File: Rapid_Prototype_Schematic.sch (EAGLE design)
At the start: 122 parts, among them IC1 OP-AMP, IC12 LM2904ITPX/NOPB, IC2 OP-AMP, IC3 OP-AMP, IC4 LM2904ITPX/NOPB, IC5 LM2904ITPX/NOPB, IC6 OP-AMP, IC7 OP-AMP

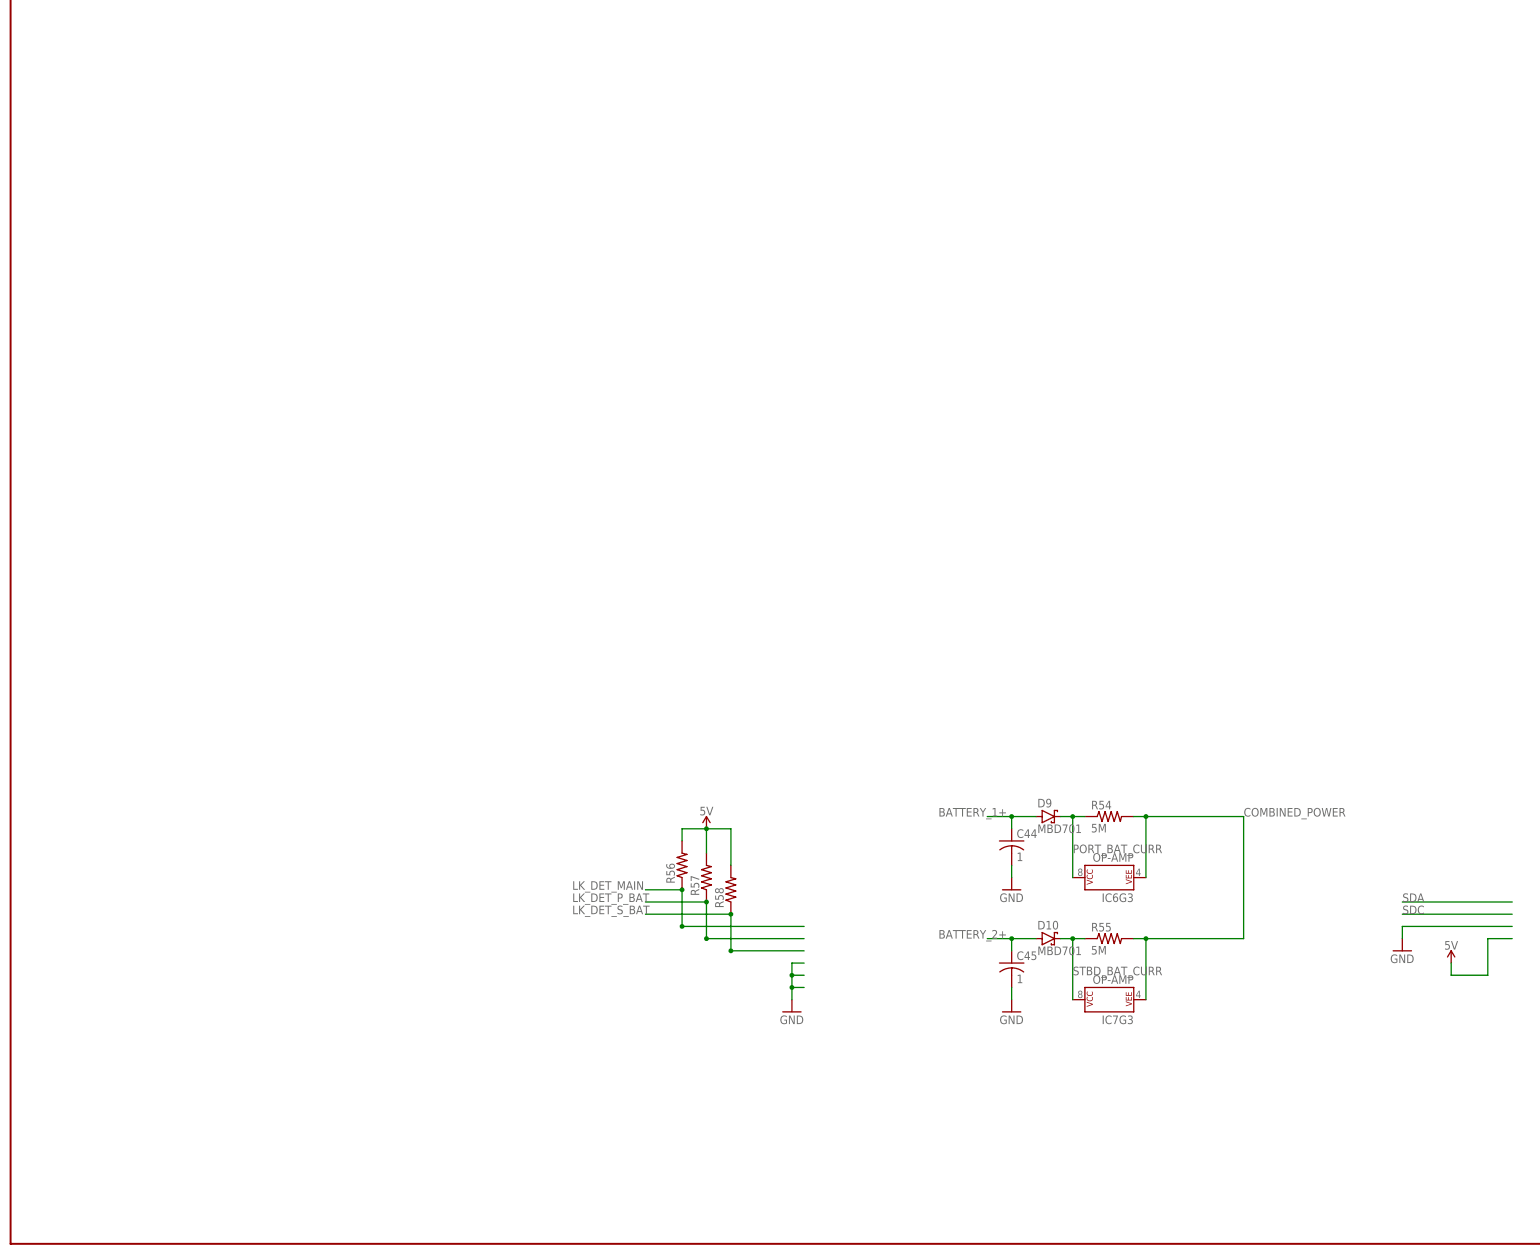
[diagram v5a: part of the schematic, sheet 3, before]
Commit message: Continued to work on the ESC modules and connected them up to each other
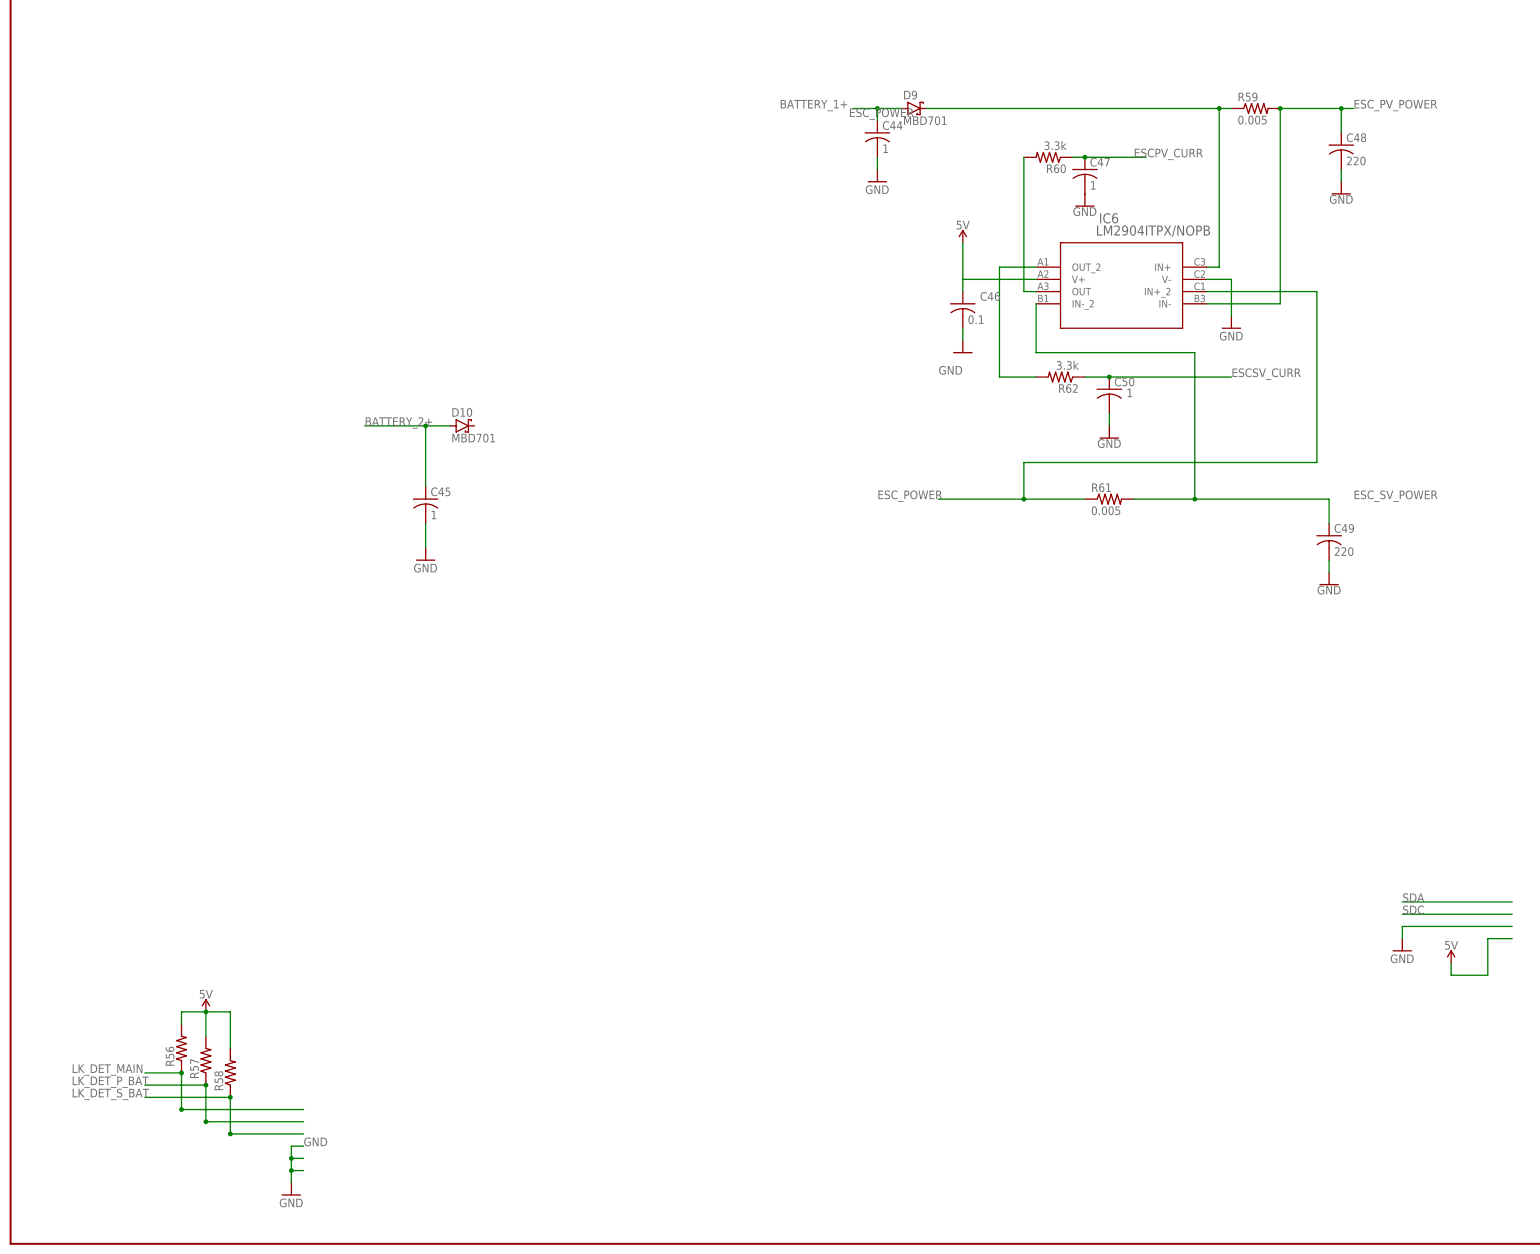
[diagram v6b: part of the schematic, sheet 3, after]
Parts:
- removed IC7: OP-AMP, SparkFun-IC-Amplifiers:OPAMP-DUALU
- removed R54, R55: 5M, adafruit:R-US_R0603
- added C46: 0.1, adafruit:C-USC0603
- added C47, C50: 1, adafruit:C-USC0805
- added C48, C49: 220, adafruit:C-US050-050X075
- added R59, R61: 0.005, adafruit:R-US_R1206
- added R60, R62: 3.3k, adafruit:R-US_R0603
- IC6: value OP-AMP -> LM2904ITPX/NOPB; device SparkFun-IC-Amplifiers:OPAMP-DUALU -> Opamp1:LM2904ITPX/NOPB
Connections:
- removed net PORT_BAT_CURR: D9.C, IC6G3.P$V+, R54.1
- removed net STBD_BAT_CURR: D10.C, IC7G3.P$V+, R55.1
- new net N$34: IC6.OUT, R60.2
- new net N$35: IC6.OUT_2, R62.2
- net 5V: now also C46.1, IC6.V+
- net COMBINED_POWER: no longer IC6G3.P$V-, IC7G3.P$V-, R54.2, R55.2
- net ESCPV_CURR: now also C47.1, R60.1
- net ESCSV_CURR: now also C50.1, R62.1
- net ESC_POWER: now also D9.C, IC6.IN+, IC6.IN+_2, R59.1, R61.1
- net ESC_PV_POWER: now also C48.1, IC6.IN-, R59.2
- net ESC_SV_POWER: now also C49.1, IC6.IN-_2, R61.2
- net GND: now also C46.2, C47.2, C48.2, C49.2, C50.2, IC6.V-
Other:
- moved on the sheet: C44, C45, D10, D9, R56, R57, R58

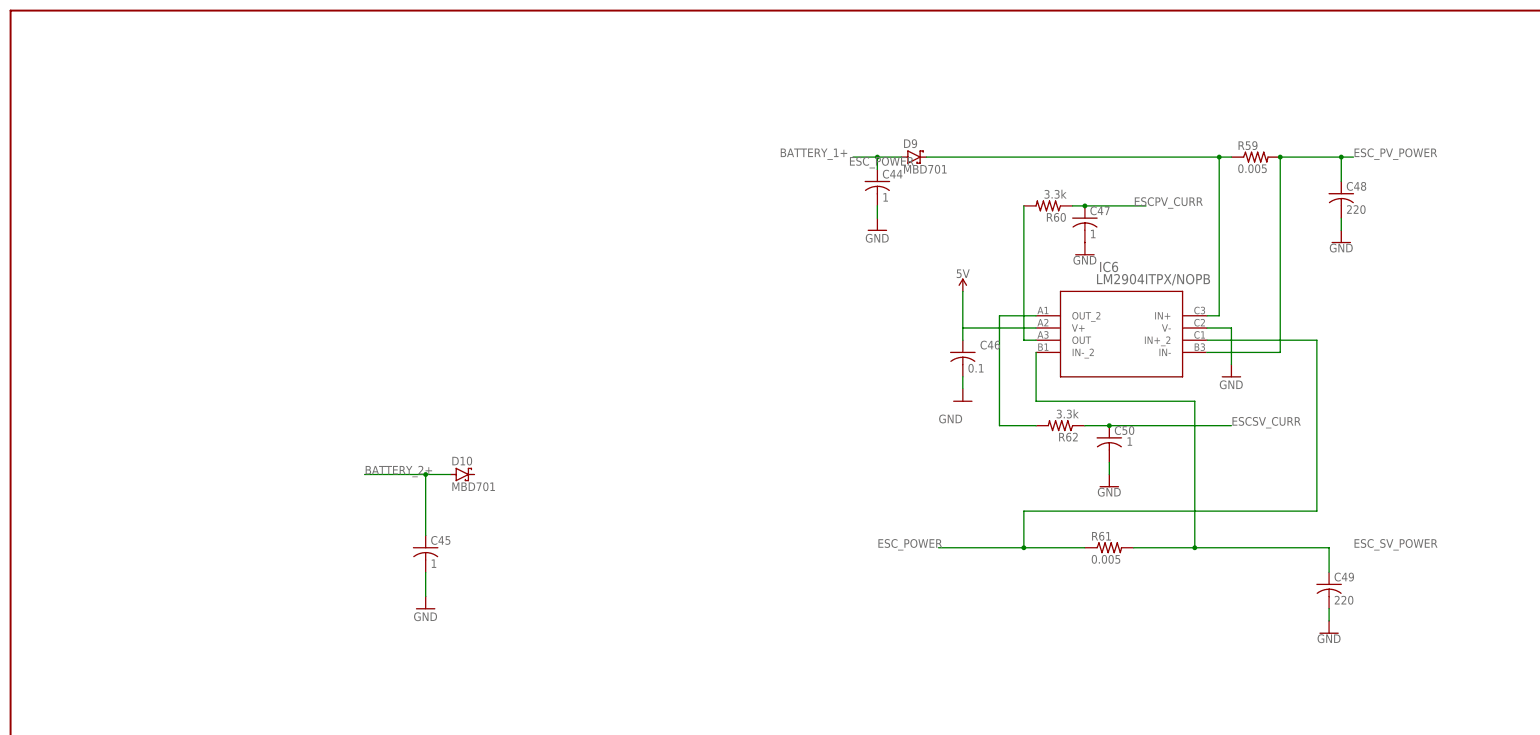
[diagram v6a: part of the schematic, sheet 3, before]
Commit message: Worked on conecting up the op amp circuit with the battery
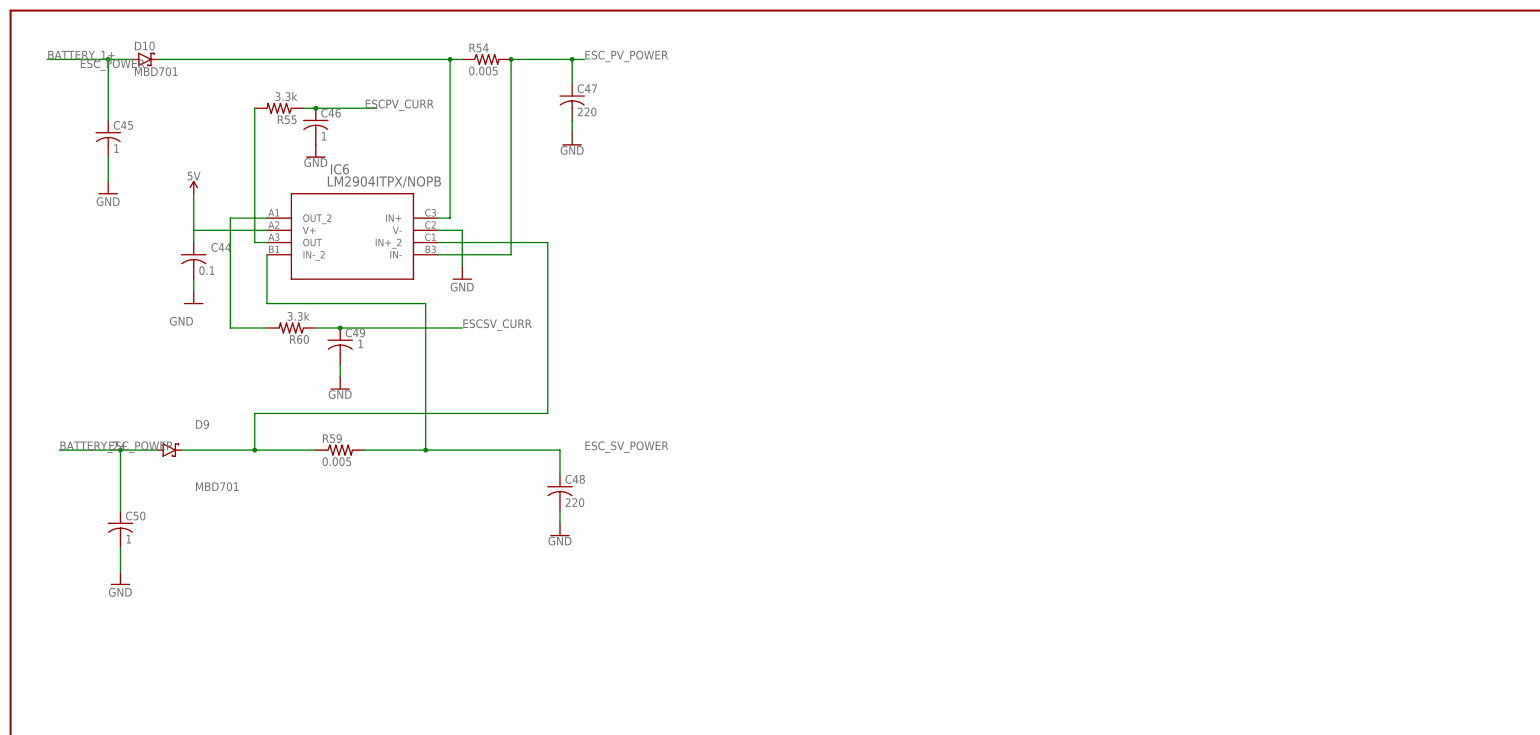
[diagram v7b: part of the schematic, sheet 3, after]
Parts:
- removed R61: 0.005, adafruit:R-US_R1206
- removed R62: 3.3k, adafruit:R-US_R0603
- added R54: 0.005, adafruit:R-US_R1206
- added R55: 3.3k, adafruit:R-US_R0603
- C44: value 1 -> 0.1
- C46: value 0.1 -> 1; device adafruit:C-USC0603 -> adafruit:C-USC0805
- C47: value 1 -> 220; device adafruit:C-USC0805 -> adafruit:C-US050-050X075
- C49: value 220 -> 1; device adafruit:C-US050-050X075 -> adafruit:C-USC0805
- C50: device adafruit:C-USC0805 -> adafruit:C-USC0603
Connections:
- net 5V: now also C44.1; no longer C46.1
- net BATTERY_1+: now also C45.1, D10.A; no longer C44.1, D9.A
- net BATTERY_2+: now also C50.1, D9.A; no longer C45.1, D10.A
- net ESCPV_CURR: now also C46.1, R55.1; no longer C47.1, R60.1
- net ESCSV_CURR: now also C49.1, R60.1; no longer C50.1, R62.1
- net ESC_POWER: now also D10.C, R54.1; no longer R61.1
- net ESC_PV_POWER: now also C47.1, R54.2; no longer C48.1, R59.2
- net ESC_SV_POWER: now also C48.1, R59.2; no longer C49.1, R61.2
- net N$34: now also R55.2; no longer R60.2
- net N$35: now also R60.2; no longer R62.2
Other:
- moved on the sheet: C44, C45, C46, C47, C48, C49, C50, D10, D9, IC6, R59, R60
